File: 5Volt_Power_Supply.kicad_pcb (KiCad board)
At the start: 2 copper layers, 12 parts, among them J1 Screw_Terminal_01x02, J2 Screw_Terminal_01x02, U1 L7805

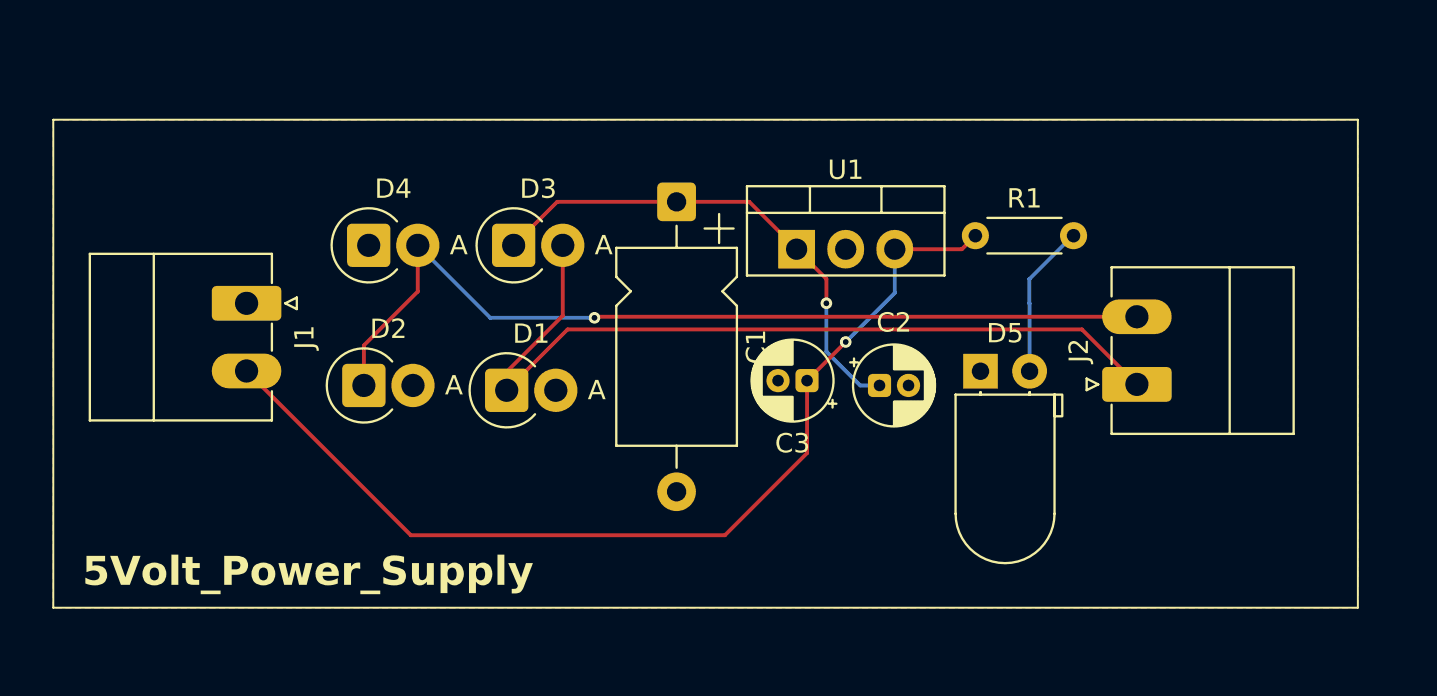
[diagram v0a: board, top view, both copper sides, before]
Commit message: Update: added front/back 2D views, copper fill views, schematic view, design rules file, updated 3D views and PCB
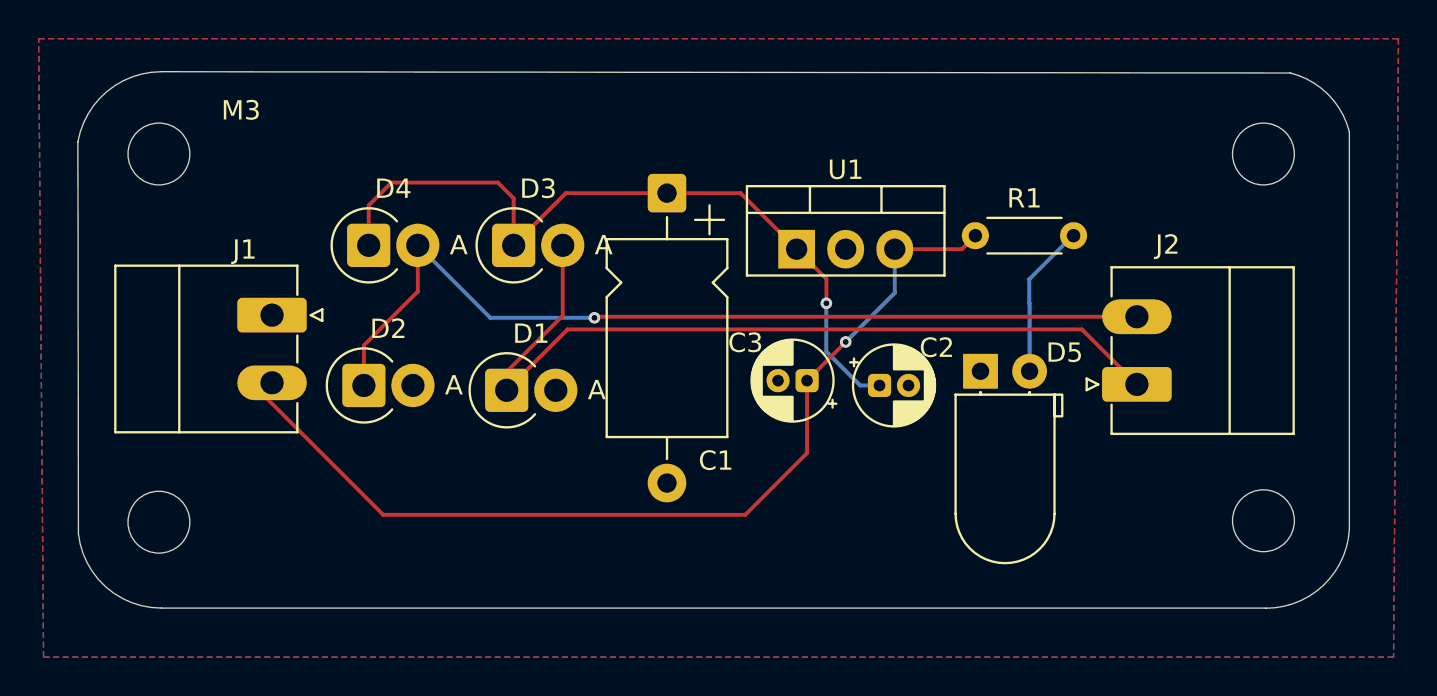
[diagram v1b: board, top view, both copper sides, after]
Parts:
- added M3: MountingHole_3.2mm_M3, MountingHole:MountingHole_3.2mm_M3, F.Cu at (101.0, 73.0)
- added M3: MountingHole_3.2mm_M3, MountingHole:MountingHole_3.2mm_M3, F.Cu at (158.1, 73.0)
- added REF**: M3, MountingHole:MountingHole_3.2mm_M3, F.Cu at (101.0, 92.1)
- added REF**: M3, MountingHole:MountingHole_3.2mm_M3, F.Cu at (158.1, 92.0)
- J1, J2: value Screw_Terminal_01x02 -> Screw_T_01x02
- moved J1 1.45 mm to (106.8, 81.4)
- moved C1 0.67 mm to (127.3, 75.0)
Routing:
- net Net-(D3-K): track 26.0 -> 39.2 mm
- net Net-(J1-Pin_2): track 51.2 -> 50.5 mm
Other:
- board outline added: 65.8 x 27.8 mm
- board text added: "5Volt_Power_Supply 1.0 Ibrahim Jarallah"
- board text removed: "5Volt_Power_Supply"
